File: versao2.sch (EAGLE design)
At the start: 22 parts

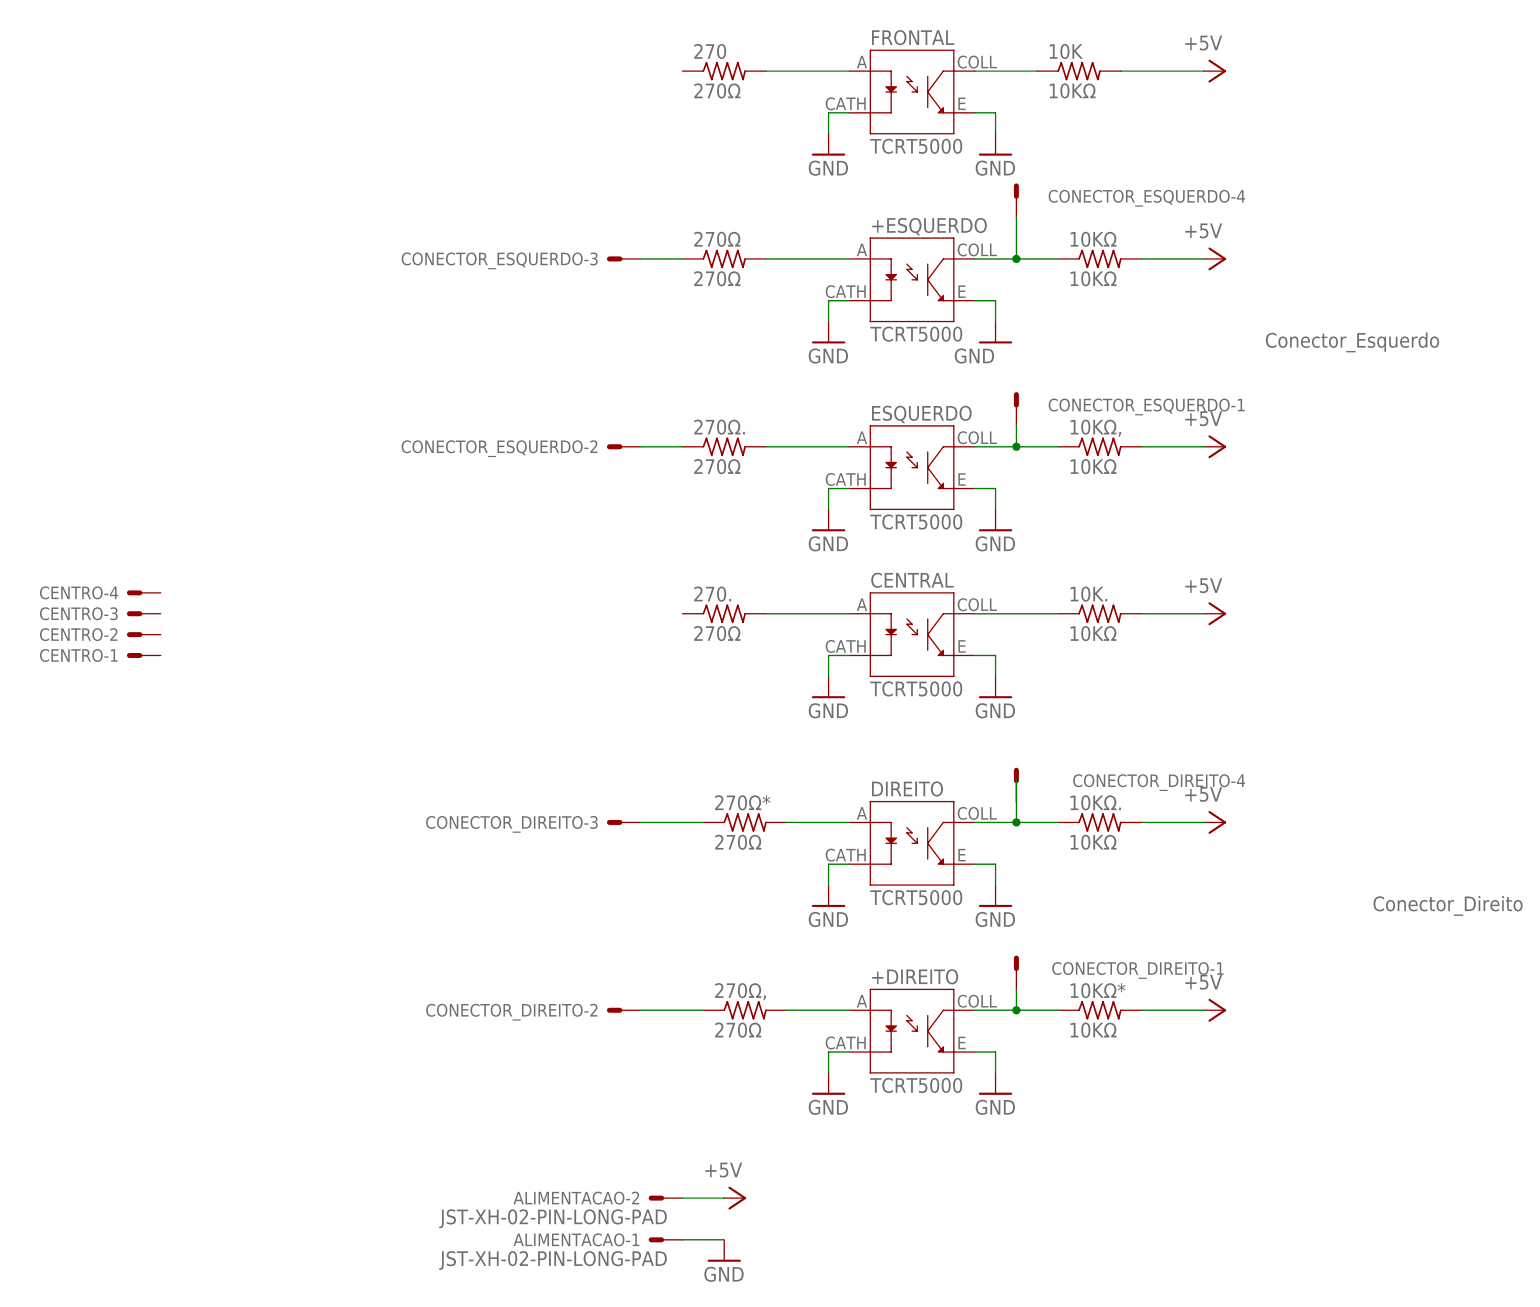
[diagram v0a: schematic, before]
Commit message: organizacao da placa com 6 sensores
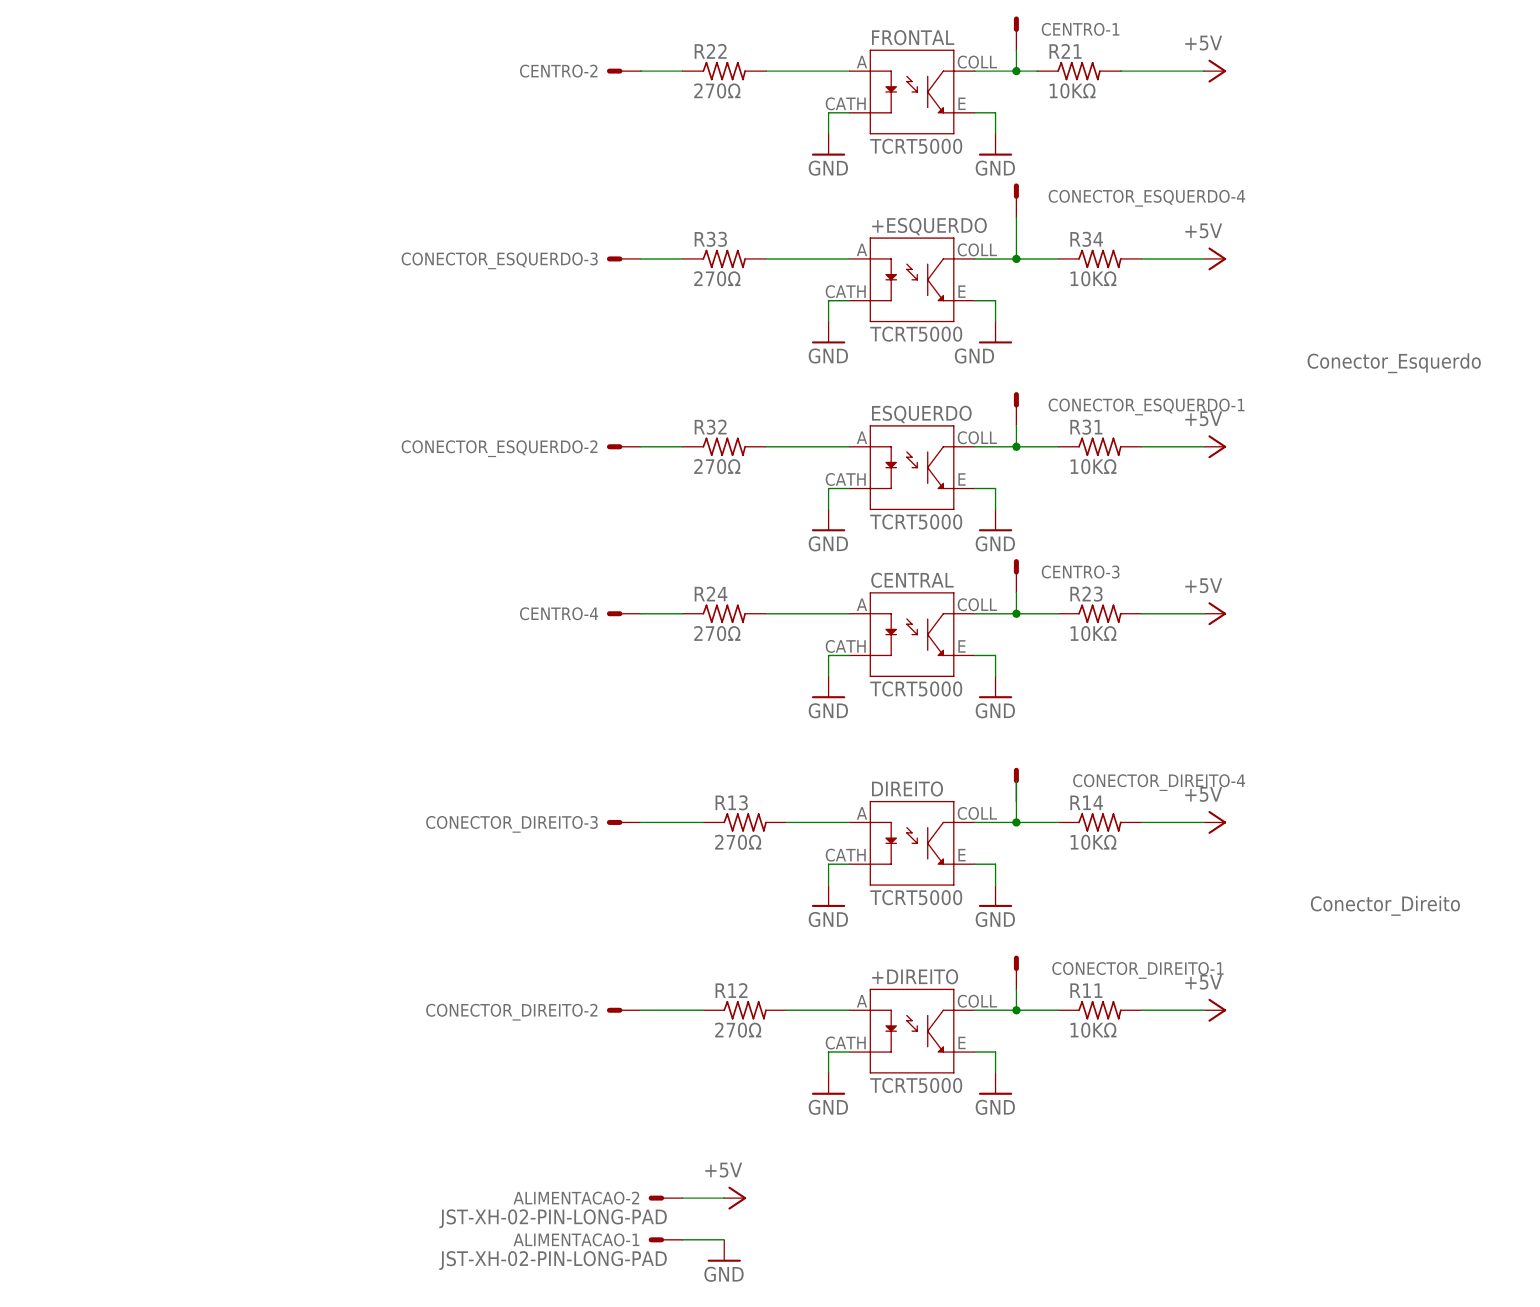
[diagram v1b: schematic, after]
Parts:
- renumbered 10K to R21, 10K. to R23, 10KΩ to R34, 10KΩ* to R11, 10KΩ, to R31, 10KΩ. to R14, 270 to R22, 270. to R24, 270Ω to R33, 270Ω* to R13, 270Ω, to R12, 270Ω. to R32
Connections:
- new net N$10: CENTRO-4.S, R24.1
- new net N$5: CENTRO-2.S, R22.1
- net N$6: now also CENTRO-3.S
- net N$8: now also CENTRO-1.S
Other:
- moved on the sheet: CENTRO-1, CENTRO-2, CENTRO-3, CENTRO-4

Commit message: adicionando os arquivos da placa de refletancia com 6 sensores.
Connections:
- net ANALOG_+ESQ. renamed ANALOG+ESQ
- net DIGITAL+ESQ. renamed DIGITAL+ESQ
- net DIGITAL_ESQ. renamed DIGITAL_ESQ
- net N$1 renamed DIGITA+ESQ
- net N$10 renamed DIGITAL_CE
- net N$2 renamed DIGITAL
- net N$3 renamed DIGTAL-DI
- net N$4 renamed DIGITAL+DIR
- net N$5 renamed FRONTAL
- net N$6 renamed ANALOG_CE
- net N$7 renamed CENTRAL
- net N$8 renamed ANALOG_FR
- net N$9 renamed DIGITAL_FR
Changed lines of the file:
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@@
 </busses>
 <nets>
-<net name="N$1" class="0">
+<net name="DIGITA+ESQ" class="0">
 <segment>
 <pinref part="R33" gate="G$1" pin="2"/>
@@
 </segment>
 </net>
-<net name="N$2" class="0">
+<net name="DIGITAL" class="0">
 <segment>
 <pinref part="R32" gate="G$1" pin="2"/>
@@
 </segment>
 </net>
-<net name="N$3" class="0">
+<net name="DIGTAL-DI" class="0">
 <segment>
 <pinref part="R13" gate="G$1" pin="2"/>
@@
 </segment>
 </net>
-<net name="N$4" class="0">
+<net name="DIGITAL+DIR" class="0">
 <segment>
 <pinref part="R12" gate="G$1" pin="2"/>
@@
 </segment>
 </net>
-<net name="ANALOG_+ESQ." class="0">
+<net name="ANALOG+ESQ" class="0">
 <segment>
 <pinref part="+ESQUERDO" gate="G$1" pin="COLL"/>
@@
 </segment>
 </net>
-<net name="DIGITAL_ESQ." class="0">
+<net name="DIGITAL_ESQ" class="0">
 <segment>
 <pinref part="R32" gate="G$1" pin="1"/>
@@
 </segment>
 </net>
-<net name="DIGITAL+ESQ." class="0">
+<net name="DIGITAL+ESQ" class="0">
 <segment>
 <pinref part="R33" gate="G$1" pin="1"/>
@@
 </segment>
 </net>
-<net name="N$6" class="0">
+<net name="ANALOG_CE" class="0">
 <segment>
 <pinref part="CENTRAL" gate="G$1" pin="COLL"/>
@@
 </segment>
 </net>
-<net name="N$7" class="0">
+<net name="CENTRAL" class="0">
 <segment>
 <pinref part="CENTRAL" gate="G$1" pin="A"/>
@@
 </segment>
 </net>
-<net name="N$8" class="0">
+<net name="ANALOG_FR" class="0">
 <segment>
 <pinref part="FRONTAL" gate="G$1" pin="COLL"/>
@@
 </segment>
 </net>
-<net name="N$9" class="0">
+<net name="DIGITAL_FR" class="0">
 <segment>
 <pinref part="FRONTAL" gate="G$1" pin="A"/>
@@
 </segment>
 </net>
-<net name="N$5" class="0">
+<net name="FRONTAL" class="0">
 <segment>
 <pinref part="CENTRO" gate="-2" pin="S"/>
@@
 </segment>
 </net>
-<net name="N$10" class="0">
+<net name="DIGITAL_CE" class="0">
 <segment>
 <pinref part="CENTRO" gate="-4" pin="S"/>
